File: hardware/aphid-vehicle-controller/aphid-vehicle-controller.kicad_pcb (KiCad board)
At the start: 4 copper layers, 19 parts, among them J1 ModICE ME-MX 24, J2 Conn_ST_STDC14, U1 STM32F405RGTx, U2 TJA1042T-3, U3 TJA1042T-3

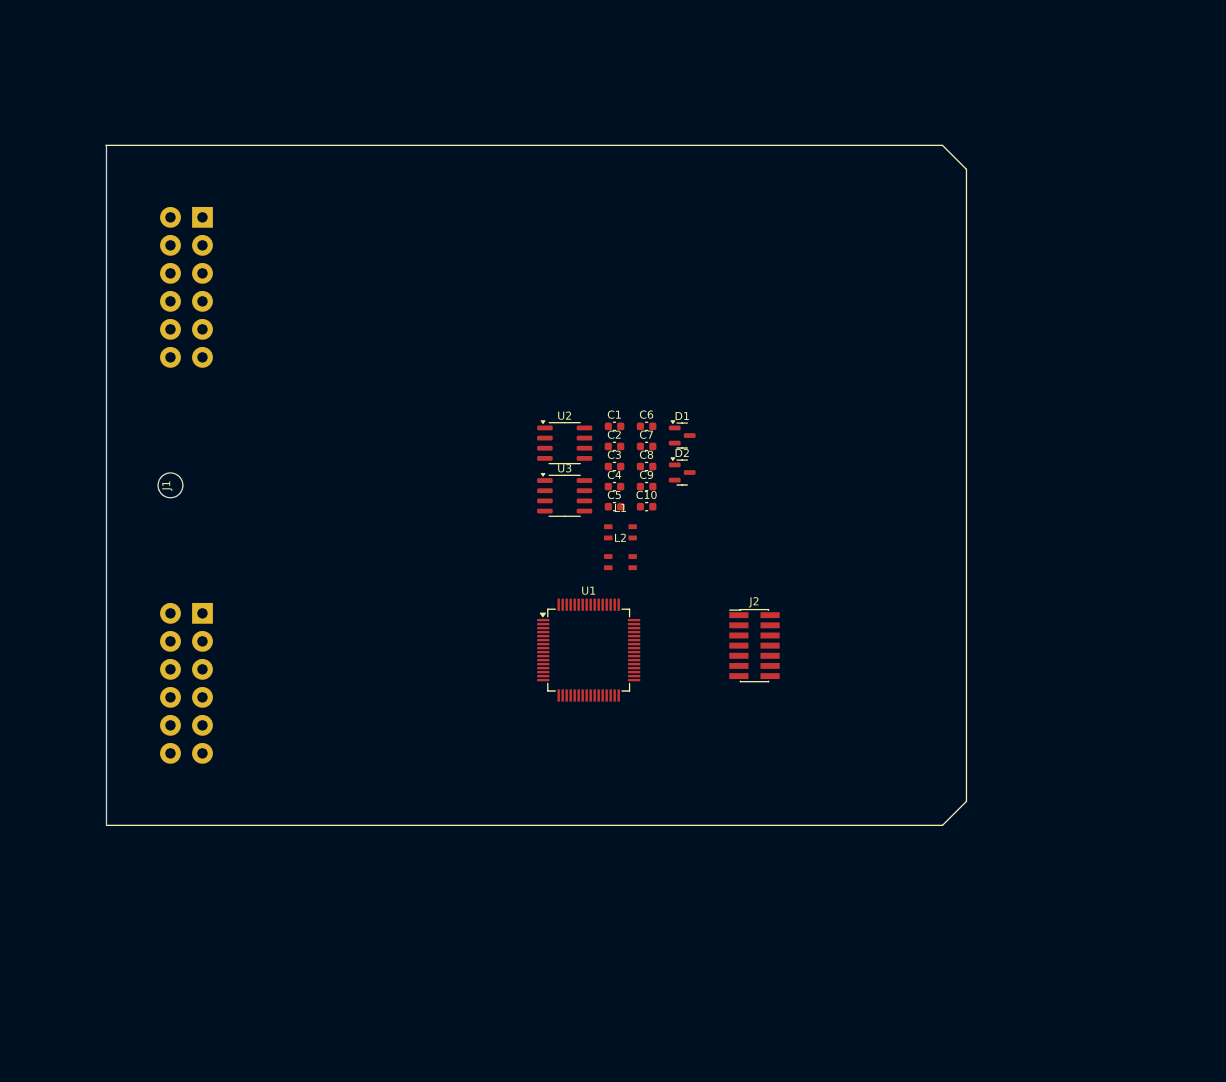
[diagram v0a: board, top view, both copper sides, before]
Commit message: feat: changed to STM32G4xx series MCU
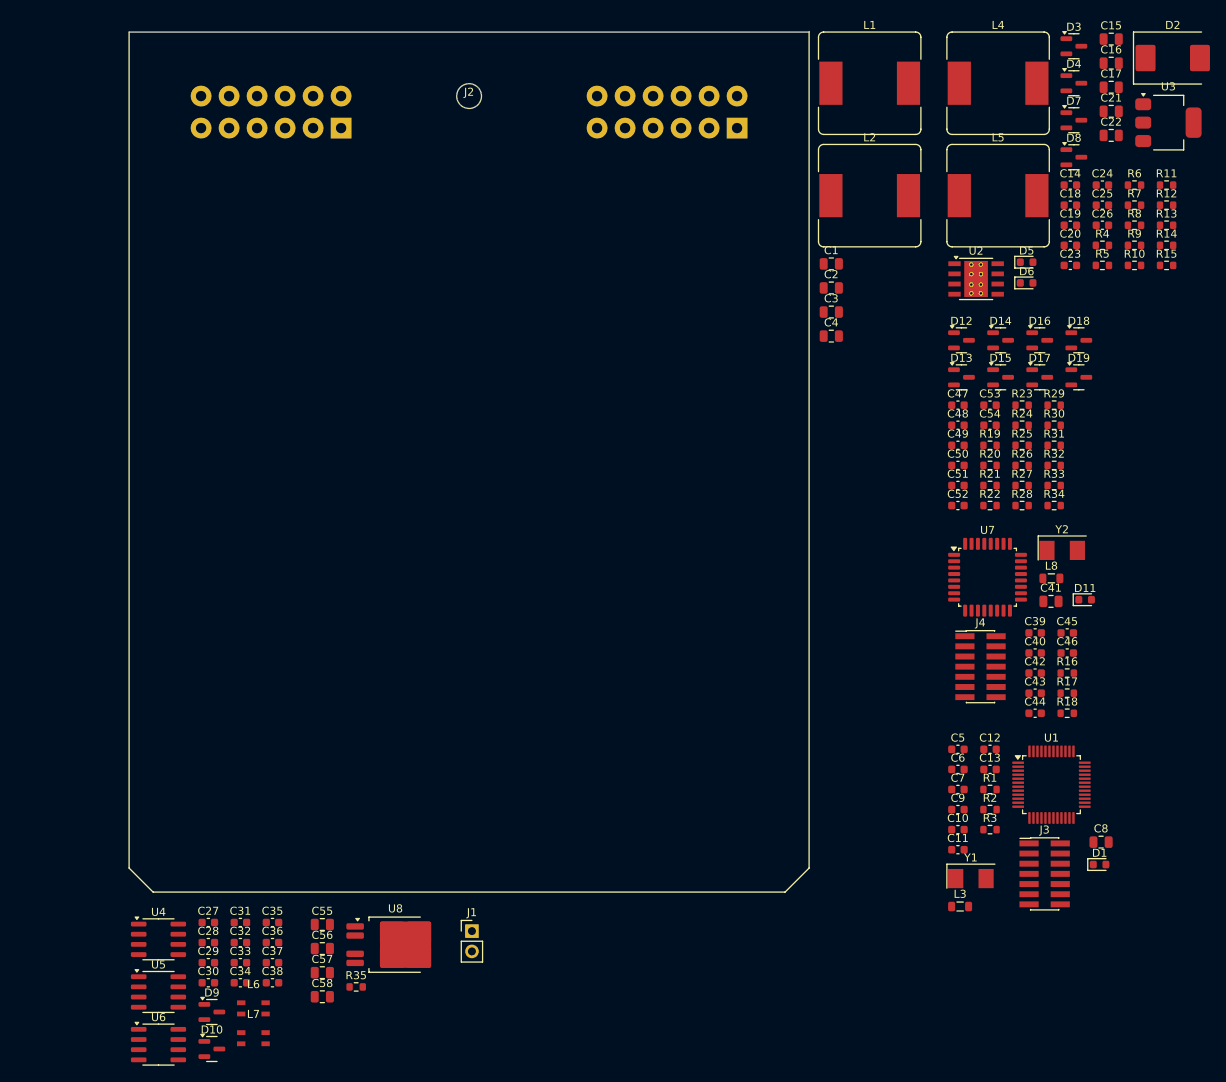
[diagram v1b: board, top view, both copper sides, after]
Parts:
- added C11: 22p, Capacitor_SMD:C_0603_1608Metric, F.Cu at (202.5, 144.2)
- added C12: 22p, Capacitor_SMD:C_0603_1608Metric, F.Cu at (206.5, 131.7)
- added C13: 100nF, Capacitor_SMD:C_0603_1608Metric, F.Cu at (206.5, 134.2)
- added C14: 10nF, Capacitor_SMD:C_0603_1608Metric, F.Cu at (216.5, 61.1)
- added C15: 10 uF, Capacitor_SMD:C_0805_2012Metric, F.Cu at (221.6, 42.9)
- added C16: 10 uF, Capacitor_SMD:C_0805_2012Metric, F.Cu at (221.6, 45.9)
- added C17: 10 uF, Capacitor_SMD:C_0805_2012Metric, F.Cu at (221.6, 48.9)
- added C18: 1 uF, Capacitor_SMD:C_0603_1608Metric, F.Cu at (216.5, 63.6)
- added C19: 100uF, Capacitor_SMD:C_0603_1608Metric, F.Cu at (216.5, 66.1)
- added C20: 1 uF, Capacitor_SMD:C_0603_1608Metric, F.Cu at (216.5, 68.7)
- added C21: 10uF, Capacitor_SMD:C_0805_2012Metric, F.Cu at (221.6, 51.9)
- added C22: 10uF, Capacitor_SMD:C_0805_2012Metric, F.Cu at (221.6, 54.9)
- added C23: 100nF, Capacitor_SMD:C_0603_1608Metric, F.Cu at (216.5, 71.2)
- added C24: 1uF, Capacitor_SMD:C_0603_1608Metric, F.Cu at (220.5, 61.1)
- added C25: 1uF, Capacitor_SMD:C_0603_1608Metric, F.Cu at (220.5, 63.6)
- added C26: 100nF, Capacitor_SMD:C_0603_1608Metric, F.Cu at (220.5, 66.1)
- added C27: 100 nF, Capacitor_SMD:C_0603_1608Metric, F.Cu at (108.8, 153.3)
- added C28: 100 nF, Capacitor_SMD:C_0603_1608Metric, F.Cu at (108.8, 155.8)
- added C29: 100 nF, Capacitor_SMD:C_0603_1608Metric, F.Cu at (108.8, 158.3)
- added C30: 33 pF, Capacitor_SMD:C_0603_1608Metric, F.Cu at (108.8, 160.8)
- added C31: 100 nF, Capacitor_SMD:C_0603_1608Metric, F.Cu at (112.8, 153.3)
- added C32: 100 nF, Capacitor_SMD:C_0603_1608Metric, F.Cu at (112.8, 155.8)
- added C33: 100 nF, Capacitor_SMD:C_0603_1608Metric, F.Cu at (112.8, 158.3)
- added C34: 33 pF, Capacitor_SMD:C_0603_1608Metric, F.Cu at (112.8, 160.8)
- added C35: 33 pF, Capacitor_SMD:C_0603_1608Metric, F.Cu at (116.8, 153.3)
- added C36: 33 pF, Capacitor_SMD:C_0603_1608Metric, F.Cu at (116.8, 155.8)
- added C37: 33 pF, Capacitor_SMD:C_0603_1608Metric, F.Cu at (116.8, 158.3)
- added C38: 33 pF, Capacitor_SMD:C_0603_1608Metric, F.Cu at (116.8, 160.8)
- added C39: 100nF, Capacitor_SMD:C_0603_1608Metric, F.Cu at (212.1, 117.1)
- added C40: 100nF, Capacitor_SMD:C_0603_1608Metric, F.Cu at (212.1, 119.6)
- added C41: 4.7uF, Capacitor_SMD:C_0805_2012Metric, F.Cu at (214.1, 113.2)
- added C42: 1uF, Capacitor_SMD:C_0603_1608Metric, F.Cu at (212.1, 122.1)
- added C43: 100nF, Capacitor_SMD:C_0603_1608Metric, F.Cu at (212.1, 124.6)
- added C44: 22p, Capacitor_SMD:C_0603_1608Metric, F.Cu at (212.1, 127.1)
- added C45: 22p, Capacitor_SMD:C_0603_1608Metric, F.Cu at (216.1, 117.1)
- added C46: 100nF, Capacitor_SMD:C_0603_1608Metric, F.Cu at (216.1, 119.6)
- added C47: 1uF, Capacitor_SMD:C_0603_1608Metric, F.Cu at (202.5, 88.6)
- added C48: 1uF, Capacitor_SMD:C_0603_1608Metric, F.Cu at (202.5, 91.1)
- added C49: 1uF, Capacitor_SMD:C_0603_1608Metric, F.Cu at (202.5, 93.7)
- added C50: 1uF, Capacitor_SMD:C_0603_1608Metric, F.Cu at (202.5, 96.2)
- added C51: 1uF, Capacitor_SMD:C_0603_1608Metric, F.Cu at (202.5, 98.7)
- added C52: 1uF, Capacitor_SMD:C_0603_1608Metric, F.Cu at (202.5, 101.2)
- added C53: 1uF, Capacitor_SMD:C_0603_1608Metric, F.Cu at (206.5, 88.6)
- added C54: 1uF, Capacitor_SMD:C_0603_1608Metric, F.Cu at (206.5, 91.1)
- added C55: 10uF, Capacitor_SMD:C_0805_2012Metric, F.Cu at (123.0, 153.6)
- added C56: 10uF, Capacitor_SMD:C_0805_2012Metric, F.Cu at (123.0, 156.6)
- added C57: 10uF, Capacitor_SMD:C_0805_2012Metric, F.Cu at (123.0, 159.6)
- added C58: 10uF, Capacitor_SMD:C_0805_2012Metric, F.Cu at (123.0, 162.6)
- added D10: NUP2105L, Package_TO_SOT_SMD:SOT-23, F.Cu at (109.2, 169.1)
- added D11: MONITOR STATUS, LED_SMD:LED_0603_1608Metric, F.Cu at (218.4, 113.0)
- added D12: BZX84C3V6, Package_TO_SOT_SMD:SOT-23, F.Cu at (202.9, 80.5)
- added D13: BZX84C3V6, Package_TO_SOT_SMD:SOT-23, F.Cu at (202.9, 85.2)
- added D14: BZX84C3V6, Package_TO_SOT_SMD:SOT-23, F.Cu at (207.8, 80.5)
- added D15: BZX84C3V6, Package_TO_SOT_SMD:SOT-23, F.Cu at (207.8, 85.2)
- added D16: BZX84C3V6, Package_TO_SOT_SMD:SOT-23, F.Cu at (212.7, 80.5)
- added D17: BZX84C3V6, Package_TO_SOT_SMD:SOT-23, F.Cu at (212.7, 85.2)
- added D18: BZX84C3V6, Package_TO_SOT_SMD:SOT-23, F.Cu at (217.6, 80.5)
- added D19: BZX84C3V6, Package_TO_SOT_SMD:SOT-23, F.Cu at (217.6, 85.2)
- added D3: BAT54C, Package_TO_SOT_SMD:SOT-23, F.Cu at (217.0, 43.8)
- added D4: BZX84C3V6, Package_TO_SOT_SMD:SOT-23, F.Cu at (217.0, 48.4)
- added D5: 5V PWR, LED_SMD:LED_0603_1608Metric, F.Cu at (211.1, 70.8)
- added D6: 3V3 PWR, LED_SMD:LED_0603_1608Metric, F.Cu at (211.1, 73.3)
- added D7: BZX84C3V6, Package_TO_SOT_SMD:SOT-23, F.Cu at (217.0, 53.0)
- added D8: BZX84C3V6, Package_TO_SOT_SMD:SOT-23, F.Cu at (217.0, 57.6)
- added D9: NUP2105L, Package_TO_SOT_SMD:SOT-23, F.Cu at (109.2, 164.5)
- added J3: MAIN_DEBUG, Connector_PinHeader_1.27mm:PinHeader_2x07_P1.27mm_Vertical_SMD, F.Cu at (213.3, 147.2)
- added J4: MONITOR_DEBUG, Connector_PinHeader_1.27mm:PinHeader_2x07_P1.27mm_Vertical_SMD, F.Cu at (205.3, 121.3)
- added L3: L, Inductor_SMD:L_0805_2012Metric, F.Cu at (202.8, 151.3)
- added L4: L, Inductor_SMD:L_Bourns_SRR1260, F.Cu at (207.5, 48.4)
- added L5: 22 uH, Inductor_SMD:L_Bourns_SRR1260, F.Cu at (207.5, 62.4)
- added L6: ACT1210D, aphid:ACT1210D, F.Cu at (114.4, 164.0)
- added L7: ACT1210D, aphid:ACT1210D, F.Cu at (114.4, 167.8)
- added L8: L, Inductor_SMD:L_0805_2012Metric, F.Cu at (214.2, 110.3)
- added R1: 22, Resistor_SMD:R_0603_1608Metric, F.Cu at (206.5, 136.7)
- added R10: 10k, Resistor_SMD:R_0603_1608Metric, F.Cu at (224.6, 71.2)
- added R11: 220, Resistor_SMD:R_0603_1608Metric, F.Cu at (228.6, 61.1)
- added R12: 38k, Resistor_SMD:R_0603_1608Metric, F.Cu at (228.6, 63.6)
- added R13: 10k, Resistor_SMD:R_0603_1608Metric, F.Cu at (228.6, 66.1)
- added R14: 38k, Resistor_SMD:R_0603_1608Metric, F.Cu at (228.6, 68.7)
- added R15: 10k, Resistor_SMD:R_0603_1608Metric, F.Cu at (228.6, 71.2)
- added R16: 22, Resistor_SMD:R_0603_1608Metric, F.Cu at (216.1, 122.1)
- added R17: 10k, Resistor_SMD:R_0603_1608Metric, F.Cu at (216.1, 124.6)
- added R18: 10k, Resistor_SMD:R_0603_1608Metric, F.Cu at (216.1, 127.1)
- added R19: 5.1k, Resistor_SMD:R_0603_1608Metric, F.Cu at (206.5, 93.7)
- added R2: 10k, Resistor_SMD:R_0603_1608Metric, F.Cu at (206.5, 139.2)
- added R20: 5.1k, Resistor_SMD:R_0603_1608Metric, F.Cu at (206.5, 96.2)
- added R21: 10k, Resistor_SMD:R_0603_1608Metric, F.Cu at (206.5, 98.7)
- added R22: 10k, Resistor_SMD:R_0603_1608Metric, F.Cu at (206.5, 101.2)
- added R23: 5.1k, Resistor_SMD:R_0603_1608Metric, F.Cu at (210.5, 88.6)
- added R24: 5.1k, Resistor_SMD:R_0603_1608Metric, F.Cu at (210.5, 91.1)
- added R25: 10k, Resistor_SMD:R_0603_1608Metric, F.Cu at (210.5, 93.7)
- added R26: 10k, Resistor_SMD:R_0603_1608Metric, F.Cu at (210.5, 96.2)
- added R27: 5.1k, Resistor_SMD:R_0603_1608Metric, F.Cu at (210.5, 98.7)
- added R28: 5.1k, Resistor_SMD:R_0603_1608Metric, F.Cu at (210.5, 101.2)
- added R29: 10k, Resistor_SMD:R_0603_1608Metric, F.Cu at (214.5, 88.6)
- added R3: 10k, Resistor_SMD:R_0603_1608Metric, F.Cu at (206.5, 141.7)
- added R30: 10k, Resistor_SMD:R_0603_1608Metric, F.Cu at (214.5, 91.1)
- added R31: 5.1k, Resistor_SMD:R_0603_1608Metric, F.Cu at (214.5, 93.7)
- added R32: 5.1k, Resistor_SMD:R_0603_1608Metric, F.Cu at (214.5, 96.2)
- added R33: 10k, Resistor_SMD:R_0603_1608Metric, F.Cu at (214.5, 98.7)
- added R34: 10k, Resistor_SMD:R_0603_1608Metric, F.Cu at (214.5, 101.2)
- added R35: R, Resistor_SMD:R_0603_1608Metric, F.Cu at (127.3, 161.3)
- added R4: R, Resistor_SMD:R_0603_1608Metric, F.Cu at (220.5, 68.7)
- added R5: 38k, Resistor_SMD:R_0603_1608Metric, F.Cu at (220.5, 71.2)
- added R6: R, Resistor_SMD:R_0603_1608Metric, F.Cu at (224.6, 61.1)
- added R7: 10k, Resistor_SMD:R_0603_1608Metric, F.Cu at (224.6, 63.6)
- added R8: 38k, Resistor_SMD:R_0603_1608Metric, F.Cu at (224.6, 66.1)
- added R9: 10k, Resistor_SMD:R_0603_1608Metric, F.Cu at (224.6, 68.7)
- added U4: TJA1042T-3, Package_SO:SOIC-8_3.9x4.9mm_P1.27mm, F.Cu at (102.6, 155.4)
- added U5: TJA1042T-3, Package_SO:SOIC-8_3.9x4.9mm_P1.27mm, F.Cu at (102.6, 162.0)
- added U6: TJA1042T-3, Package_SO:SOIC-8_3.9x4.9mm_P1.27mm, F.Cu at (102.6, 168.6)
- added U7: STM32G431KBTx, Package_QFP:LQFP-32_7x7mm_P0.8mm, F.Cu at (206.2, 110.1)
- added U8: BTS6143D, Package_TO_SOT_SMD:TO-252-4, F.Cu at (132.2, 156.1)
- added Y1: 8 MHz, aphid:ABM3-x.xxxMHZ-D2Y-T, F.Cu at (204.1, 147.8)
- added Y2: 8 MHz, aphid:ABM3-x.xxxMHZ-D2Y-T, F.Cu at (215.5, 106.8)
- C1, C2, C3, C4: value 33 pF -> 10uF; footprint Capacitor_SMD:C_0603_1608Metric -> Capacitor_SMD:C_0805_2012Metric
- C10, C7: value 100 nF -> 100nF
- C5, C6: value 33 pF -> 100nF
- C8: value 100 nF -> 4.7uF; footprint Capacitor_SMD:C_0603_1608Metric -> Capacitor_SMD:C_0805_2012Metric
- C9: value 100 nF -> 1uF
- D1: value NUP2105L -> STATUS; footprint Package_TO_SOT_SMD:SOT-23 -> LED_SMD:LED_0603_1608Metric
- D2: value NUP2105L -> B340; footprint Package_TO_SOT_SMD:SOT-23 -> Diode_SMD:D_SMC
- J1: value ModICE ME-MX 24 -> MONITOR UART; footprint aphid-vehicle-controller:ModICE_ME-MX_24 -> Connector_PinHeader_2.54mm:PinHeader_1x02_P2.54mm_Vertical
- J2: value Conn_ST_STDC14 -> ModICE ME-MX 24; footprint Connector_PinHeader_1.27mm:PinHeader_2x07_P1.27mm_Vertical_SMD -> aphid:ModICE_ME-MX_24
- L1, L2: value ACT1210D -> L; footprint aphid-vehicle-controller:ACT1210D -> Inductor_SMD:L_Bourns_SRR1260
- U1: value STM32F405RGTx -> STM32G491CETx; footprint Package_QFP:LQFP-64_10x10mm_P0.5mm -> Package_QFP:LQFP-48_7x7mm_P0.5mm
- U2: value TJA1042T-3 -> TPS5430DDA; footprint Package_SO:SOIC-8_3.9x4.9mm_P1.27mm -> Package_SO:TI_SO-PowerPAD-8_ThermalVias
- U3: value TJA1042T-3 -> AMS1117-3.3; footprint Package_SO:SOIC-8_3.9x4.9mm_P1.27mm -> Package_TO_SOT_SMD:SOT-223-3_TabPin2
- moved U3 88.7 mm to (228.8, 53.3)
- moved D2 80.3 mm to (229.3, 45.2)
- moved J2 77.4 mm to (141.4, 50.0)
- moved D1 74.8 mm to (220.2, 146.1)
- moved C8 73.7 mm to (220.4, 143.2)
- moved J1 67.3 mm to (141.7, 154.4), turned to 0 degrees
- moved L1 64.2 mm to (191.5, 48.4)
- moved U1 60.2 mm to (214.2, 136.1)
- moved C6 57.9 mm to (202.5, 134.2)
- moved C7 57.9 mm to (202.5, 136.7)
- moved C10 56.1 mm to (202.5, 141.7)
- moved C9 56.1 mm to (202.5, 139.2)
- moved L2 55.4 mm to (191.5, 62.4)
- moved U2 55.4 mm to (204.8, 72.9)
- moved C5 52.6 mm to (202.5, 131.7)
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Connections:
- C1 pad 1: Net-(U2-CANH) -> Net-(J2A-L9)
- C10 pad 1: +3.3V -> /MCU/MAIN_VDDA
- C2 pad 1: Net-(U2-CANH) -> +5V
- C2 pad 2: Net-(U2-CANL) -> GND
- C3 pad 1: Net-(U2-CANL) -> Net-(J2B-R9)
- C4 pad 1: Net-(U3-CANH) -> +5V
- C5 pad 1: Net-(U3-CANL) -> +3.3V
- C6 pad 1: Net-(U3-CANH) -> +3.3V
- C6 pad 2: Net-(U3-CANL) -> GND
- C7 pad 1: +5V -> +3.3V
- C8 pad 1: +5V -> +3.3V
- C9 pad 1: +3.3V -> /MCU/MAIN_VDDA
- D1 pad 1: Net-(U2-CANH) -> GND
- D1 pad 2: Net-(U2-CANL) -> Net-(D1-A)
- D2 pad 1: Net-(U3-CANH) -> Net-(D2-K)
- D2 pad 2: Net-(U3-CANL) -> GND
- J1 pad 1: GND -> /MCU/MONITOR_UART_TX
- J1 pad 2: /CAN/CAN1_LOW -> /MCU/MONITOR_UART_RX
- J2 pad 1: unconnected-(J2-NC-Pad1) -> GND
- J2 pad 10: unconnected-(J2-JTDI/NC-Pad10) -> /Connectors/ACC2
- J2 pad 11: unconnected-(J2-GNDDetect-Pad11) -> /Connectors/ACC1
- J2 pad 12: unconnected-(J2-~{RST}-Pad12) -> /Connectors/VIN
- J2 pad 13: unconnected-(J2-VCP_RX-Pad13) -> GND
- J2 pad 14: unconnected-(J2-VCP_TX-Pad14) -> /CAN/CAN2_LOW
- J2 pad 2: unconnected-(J2-NC-Pad2) -> /CAN/CAN1_LOW
- J2 pad 3: unconnected-(J2-VCC-Pad3) -> /CAN/CAN1_HIGH
- J2 pad 4: unconnected-(J2-JTMS/SWDIO-Pad4) -> /Connectors/BRAKE2
- J2 pad 5: Net-(J2-GND-Pad5) -> /Connectors/BRAKE1
- J2 pad 6: unconnected-(J2-JCLK/SWCLK-Pad6) -> /Connectors/VIN
- J2 pad 7: Net-(J2-GND-Pad5) -> GND
- J2 pad 9: unconnected-(J2-JRCLK/NC-Pad9) -> Net-(J2A-L9)
- L1 pad 1: Net-(U2-CANH) -> +5V
- L1 pad 2: Net-(U2-CANL) -> Net-(J2A-L9)
- L2 pad 1: Net-(U3-CANH) -> +5V
- L2 pad 2: Net-(U3-CANL) -> Net-(J2B-R9)
- U1 pad 1: unconnected-(U1-VBAT-Pad1) -> +3.3V
- U1 pad 16: unconnected-(U1-PA2-Pad16) -> /MCU/POWER_KEEPALIVE
- U1 pad 18: Net-(U1-VSS-Pad18) -> unconnected-(U1-PB2-Pad18)
- U1 pad 19: unconnected-(U1-VDD-Pad19) -> GND
- U1 pad 20: unconnected-(U1-PA4-Pad20) -> /MCU/MAIN_VDDA
- U1 pad 21: unconnected-(U1-PA5-Pad21) -> /MCU/MAIN_VDDA
- U1 pad 22: unconnected-(U1-PA6-Pad22) -> /MCU/MAIN_DBG_TX
- U1 pad 23: unconnected-(U1-PA7-Pad23) -> GND
- U1 pad 24: unconnected-(U1-PC4-Pad24) -> +3.3V
- U1 pad 25: unconnected-(U1-PC5-Pad25) -> /MCU/MAIN_DBG_RX
- U1 pad 26: unconnected-(U1-PB0-Pad26) -> /CAN/CAN2_RX
- U1 pad 27: unconnected-(U1-PB1-Pad27) -> /CAN/CAN2_TX
- U1 pad 31: unconnected-(U1-VCAP_1-Pad31) -> /MCU/MONITOR_UART_TX
- U1 pad 32: unconnected-(U1-VDD-Pad32) -> /MCU/MONITOR_UART_RX
- U1 pad 33: unconnected-(U1-PB12-Pad33) -> /CAN/CAN1_RX
- U1 pad 34: unconnected-(U1-PB13-Pad34) -> /CAN/CAN1_TX
- U1 pad 35: unconnected-(U1-PB14-Pad35) -> GND
- U1 pad 36: unconnected-(U1-PB15-Pad36) -> +3.3V
- U1 pad 37: unconnected-(U1-PC6-Pad37) -> /MCU/MAIN_SWDIO
- U1 pad 38: unconnected-(U1-PC7-Pad38) -> /MCU/MAIN_SWCLK
- U1 pad 40: unconnected-(U1-PC9-Pad40) -> /MCU/MAIN_SWO
- U1 pad 47: unconnected-(U1-VCAP_2-Pad47) -> GND
- U1 pad 48: unconnected-(U1-VDD-Pad48) -> +3.3V
- U1 pad 5: unconnected-(U1-PH0-Pad5) -> /MCU/MAIN_OSC_IN
- U1 pad 6: unconnected-(U1-PH1-Pad6) -> /MCU/MAIN_OSC_OUT
- U1 pad 7: unconnected-(U1-NRST-Pad7) -> /MCU/MAIN_NRST
- U2 pad 1: /CAN/CAN1_TX -> Net-(U2-BOOT)
- U2 pad 2: GND -> unconnected-(U2-NC-Pad2)
- U2 pad 3: +5V -> unconnected-(U2-NC-Pad3)
- U2 pad 4: /CAN/CAN1_RX -> Net-(U2-VSENSE)
- U2 pad 5: +3.3V -> Net-(U2-EN)
- U2 pad 6: Net-(U2-CANL) -> GND
- U2 pad 7: Net-(U2-CANH) -> +12V
- U2 pad 8: GND -> Net-(D2-K)
- U3 pad 1: /CAN/CAN2_TX -> GND
- U3 pad 2: GND -> +3.3V

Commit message: feat: changed to a more modern DCDC
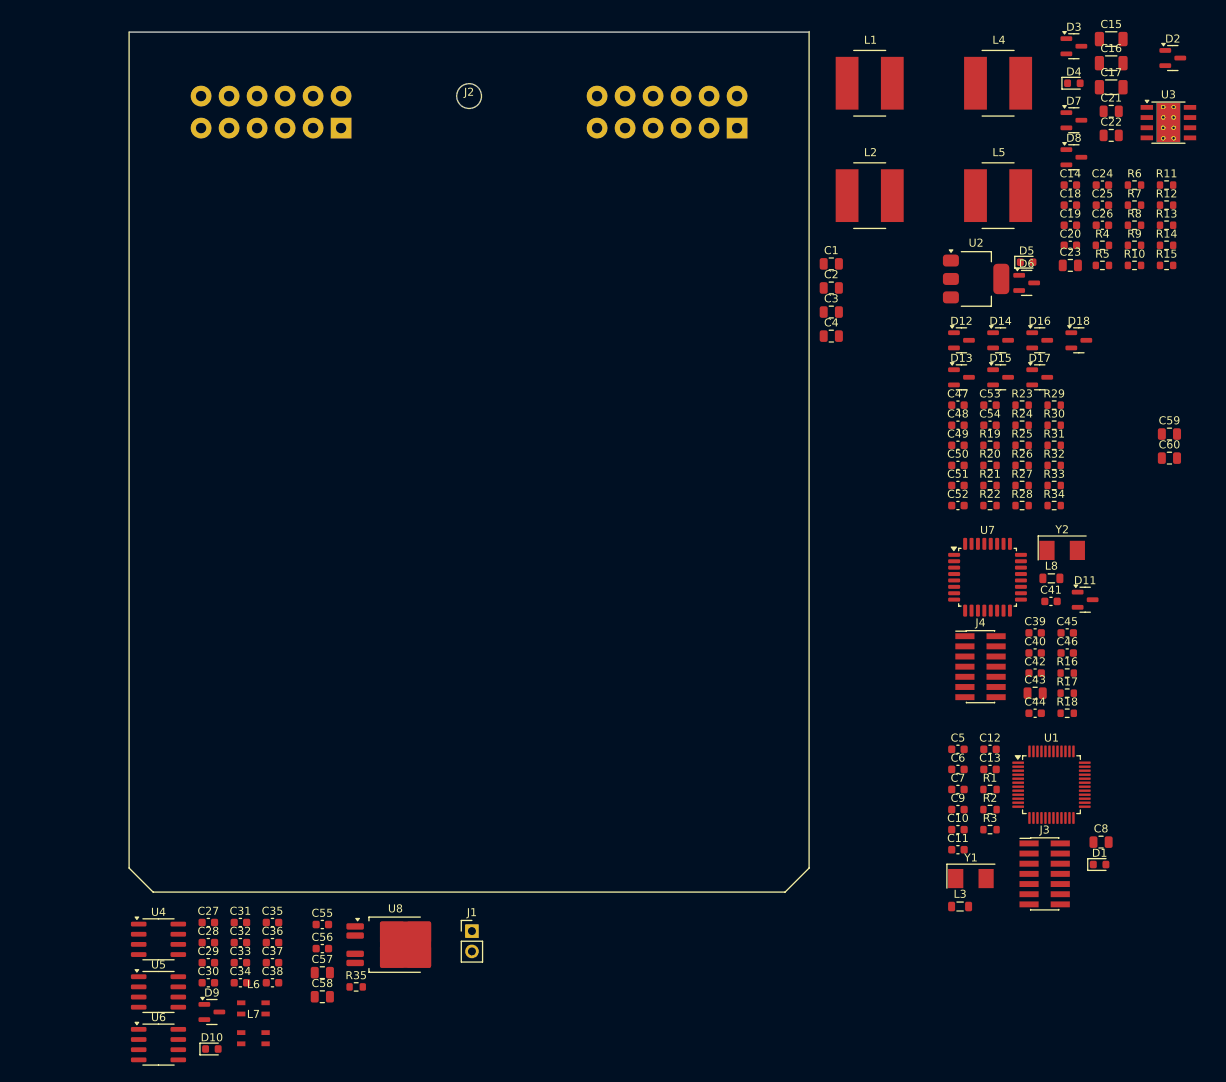
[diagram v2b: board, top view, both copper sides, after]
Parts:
- removed D19: BZX84C3V6, Package_TO_SOT_SMD:SOT-23
- added C59: 10uF, Capacitor_SMD:C_0805_2012Metric, F.Cu at (228.9, 92.2)
- added C60: 10uF, Capacitor_SMD:C_0805_2012Metric, F.Cu at (228.9, 95.2)
- C14: value 10nF -> 100nF
- C15, C16, C17: value 10 uF -> 10 uF 50V; footprint Capacitor_SMD:C_0805_2012Metric -> Capacitor_SMD:C_1206_3216Metric
- C18, C20: value 1 uF -> 100nF
- C19: value 100uF -> 6.8pF
- C21, C22: value 10uF -> 22uF
- C23: value 100nF -> 22uF; footprint Capacitor_SMD:C_0603_1608Metric -> Capacitor_SMD:C_0805_2012Metric
- C25, C42, C48: value 1uF -> 100nF
- C26: value 100nF -> 1uF
- C27: value 100 nF -> 1uF
- C28: value 100 nF -> 100nF
- C30, C34, C35: value 33 pF -> 100 nF
- C32: value 100 nF -> 33 pF
- C39, C40: value 100nF -> 33 pF
- C41: value 4.7uF -> 100nF; footprint Capacitor_SMD:C_0805_2012Metric -> Capacitor_SMD:C_0603_1608Metric
- C43: value 100nF -> 4.7uF; footprint Capacitor_SMD:C_0603_1608Metric -> Capacitor_SMD:C_0805_2012Metric
- C44: value 22p -> 1uF
- C45: value 22p -> 100nF
- C46: value 100nF -> 22p
- C47: value 1uF -> 22p
- C55, C56: value 10uF -> 1uF; footprint Capacitor_SMD:C_0805_2012Metric -> Capacitor_SMD:C_0603_1608Metric
- D10: value NUP2105L -> MONITOR STATUS; footprint Package_TO_SOT_SMD:SOT-23 -> LED_SMD:LED_0603_1608Metric
- D11: value MONITOR STATUS -> BZX84C3V6; footprint LED_SMD:LED_0603_1608Metric -> Package_TO_SOT_SMD:SOT-23
- D2: value B340 -> BAT54C; footprint Diode_SMD:D_SMC -> Package_TO_SOT_SMD:SOT-23
- D3: value BAT54C -> BZX84C3V6
- D4: value BZX84C3V6 -> 5V PWR; footprint Package_TO_SOT_SMD:SOT-23 -> LED_SMD:LED_0603_1608Metric
- D5: value 5V PWR -> 3V3 PWR
- D6: value 3V3 PWR -> BZX84C3V6; footprint LED_SMD:LED_0603_1608Metric -> Package_TO_SOT_SMD:SOT-23
- D8: value BZX84C3V6 -> NUP2105L
- L1, L2, L4: value L -> 2.2uH; footprint Inductor_SMD:L_Bourns_SRR1260 -> Inductor_SMD:L_Bourns_SRN8040TA
- L5: value 22 uH -> 2.2uH; footprint Inductor_SMD:L_Bourns_SRR1260 -> Inductor_SMD:L_Bourns_SRN8040TA
- R4: value R -> 100k
- R5: value 38k -> 24.9k
- R6: value R -> 38k
- U2: value TPS5430DDA -> AMS1117-3.3; footprint Package_SO:TI_SO-PowerPAD-8_ThermalVias -> Package_TO_SOT_SMD:SOT-223-3_TabPin2
- U3: value AMS1117-3.3 -> LMR33630BDDA; footprint Package_TO_SOT_SMD:SOT-223-3_TabPin2 -> Package_SO:Texas_HSOP-8-1EP_3.9x4.9mm_P1.27mm_ThermalVias
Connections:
- C14 pad 1: Net-(U2-BOOT) -> Net-(U3-BOOT)
- C14 pad 2: Net-(D2-K) -> Net-(U3-SW)
- C19 pad 2: GND -> Net-(U3-FB)
- C22 pad 1: +3.3V -> +5V
- C23 pad 1: Net-(U2-EN) -> +3.3V
- C24 pad 1: /MCU/VIN_SENSE -> Net-(U3-VCC)
- C25 pad 1: /MCU/IGNITION_SENSE -> Net-(U3-EN)
- C26 pad 1: /MCU/CRANK_SENSE -> /MCU/VIN_SENSE
- C27 pad 1: +5V -> /MCU/IGNITION_SENSE
- C28 pad 1: +5V -> /MCU/CRANK_SENSE
- C30 pad 1: Net-(U4-CANH) -> +5V
- C30 pad 2: Net-(U4-CANL) -> GND
- C31 pad 1: +3.3V -> +5V
- C32 pad 1: +3.3V -> Net-(U4-CANH)
- C32 pad 2: GND -> Net-(U4-CANL)
- C34 pad 1: Net-(U4-CANH) -> +3.3V
- C35 pad 1: Net-(U4-CANL) -> +3.3V
- C36 pad 1: Net-(U6-CANH) -> Net-(U4-CANH)
- C36 pad 2: Net-(U6-CANL) -> GND
- C37 pad 1: Net-(U6-CANH) -> Net-(U4-CANL)
- C38 pad 1: Net-(U6-CANL) -> Net-(U6-CANH)
- C38 pad 2: GND -> Net-(U6-CANL)
- C39 pad 1: +3.3V -> Net-(U6-CANH)
- C40 pad 1: +3.3V -> Net-(U6-CANL)
- C42 pad 1: /Monitor/MONITOR_VDDA -> +3.3V
- C43 pad 1: /Monitor/MONITOR_VDDA -> +3.3V
- C44 pad 1: /Monitor/MONITOR_OSC_IN -> /Monitor/MONITOR_VDDA
- C45 pad 1: Net-(C45-Pad1) -> /Monitor/MONITOR_VDDA
- C46 pad 1: /Monitor/MONITOR_NRST -> /Monitor/MONITOR_OSC_IN
- C47 pad 1: /Inputs/BRAKE1_FILTERED -> Net-(C47-Pad1)
- C48 pad 1: /Inputs/ACC1_FILTERED -> /Monitor/MONITOR_NRST
- C49 pad 1: /Inputs/BRAKE2_FILTERED -> /Inputs/BRAKE1_FILTERED
- C50 pad 1: /Inputs/ACC2_FILTERED -> /Inputs/ACC1_FILTERED
- C51 pad 1: /Inputs/DIR_F1_FILTERED -> /Inputs/BRAKE2_FILTERED
- C52 pad 1: /Inputs/DIR_R1_FILTERED -> /Inputs/ACC2_FILTERED
- C53 pad 1: /Inputs/DIR_F2_FILTERED -> /Inputs/DIR_F1_FILTERED
- C54 pad 1: /Inputs/DIR_R2_FILTERED -> /Inputs/DIR_R1_FILTERED
- C55 pad 1: +12V -> /Inputs/DIR_F2_FILTERED
- C56 pad 1: +12V -> /Inputs/DIR_R2_FILTERED
- D10 pad 1: Net-(U6-CANH) -> GND
- D10 pad 2: Net-(U6-CANL) -> Net-(D10-A)
- D11 pad 2: Net-(D11-A) -> unconnected-(D11-NC-Pad2)
- D12 pad 3: /Inputs/BRAKE1_FILTERED -> /Inputs/ACC1_FILTERED
- D13 pad 3: /Inputs/ACC1_FILTERED -> /Inputs/BRAKE2_FILTERED
- D14 pad 3: /Inputs/BRAKE2_FILTERED -> /Inputs/ACC2_FILTERED
- D15 pad 3: /Inputs/ACC2_FILTERED -> /Inputs/DIR_F1_FILTERED
- D16 pad 3: /Inputs/DIR_F1_FILTERED -> /Inputs/DIR_R1_FILTERED
- D17 pad 3: /Inputs/DIR_R1_FILTERED -> /Inputs/DIR_F2_FILTERED
- D18 pad 3: /Inputs/DIR_F2_FILTERED -> /Inputs/DIR_R2_FILTERED
- D2 pad 1: Net-(D2-K) -> /MCU/POWER_KEEPALIVE
- D2 pad 2: GND -> Net-(D2-Pad2)
- D3 pad 1: /MCU/POWER_KEEPALIVE -> GND
- D3 pad 2: Net-(D3-Pad2) -> unconnected-(D3-NC-Pad2)
- D3 pad 3: Net-(U2-EN) -> /MCU/VIN_SENSE
- D4 pad 2: unconnected-(D4-NC-Pad2) -> Net-(D4-A)
- D6 pad 2: Net-(D6-A) -> unconnected-(D6-NC-Pad2)
- D7 pad 3: /MCU/IGNITION_SENSE -> /MCU/CRANK_SENSE
- D8 pad 1: GND -> Net-(U4-CANH)
- D8 pad 2: unconnected-(D8-NC-Pad2) -> Net-(U4-CANL)
- D8 pad 3: /MCU/CRANK_SENSE -> GND
- D9 pad 1: Net-(U4-CANH) -> Net-(U6-CANH)
- D9 pad 2: Net-(U4-CANL) -> Net-(U6-CANL)
- L1 pad 1: +5V -> Net-(J2A-L9)
- L1 pad 2: Net-(J2A-L9) -> +5V
- L2 pad 1: +5V -> Net-(J2B-R9)
- L2 pad 2: Net-(J2B-R9) -> +5V
- L5 pad 1: Net-(D2-K) -> Net-(U3-SW)
- R10 pad 1: Net-(D5-A) -> Net-(D4-A)
- R11 pad 1: Net-(D6-A) -> Net-(D5-A)
- R16 pad 1: Net-(C45-Pad1) -> Net-(C47-Pad1)
- R18 pad 1: Net-(D11-A) -> Net-(D10-A)
- R4 pad 2: Net-(U2-VSENSE) -> Net-(U3-FB)
- R5 pad 1: Net-(D3-Pad2) -> Net-(U3-FB)
- R5 pad 2: /Connectors/IGNITION -> GND
- R6 pad 1: Net-(U2-VSENSE) -> Net-(D2-Pad2)
- R6 pad 2: GND -> /Connectors/IGNITION
- R7 pad 2: Net-(U2-EN) -> Net-(U3-EN)
- U2 pad 1: Net-(U2-BOOT) -> GND
- U2 pad 2: unconnected-(U2-NC-Pad2) -> +3.3V
- U2 pad 3: unconnected-(U2-NC-Pad3) -> +5V
- U3 pad 2: +3.3V -> +12V
- U3 pad 3: +5V -> Net-(U3-EN)
- Y2 pad 2: Net-(C45-Pad1) -> Net-(C47-Pad1)

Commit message: worked on routing
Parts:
- C31, C34, C35: value 100 nF -> 33 pF
- C32, C36, C37: value 33 pF -> 100 nF
- J3, J4: moved to B.Cu
- moved R13 127.2 mm to (107.1, 104.1)
- moved R12 126.0 mm to (106.7, 95.7), turned to 90 degrees
- moved R15 122.6 mm to (110.5, 104.1)
- moved R14 121.1 mm to (110.5, 95.7), turned to 90 degrees
- moved L6 117.2 mm to (170.2, 61.0), turned to 90 degrees
- moved D7 116.5 mm to (110.5, 100.3), turned to 90 degrees
- moved C34 108.5 mm to (165.6, 66.0)
- moved D6 107.8 mm to (106.7, 100.3), turned to 90 degrees
- moved C39 107.4 mm to (115.1, 71.1)
- moved L7 106.7 mm to (120.1, 61.2), turned to 90 degrees
- moved C3 105.0 mm to (87.6, 42.2), turned to -90 degrees
- moved C4 104.3 mm to (87.6, 47.3), turned to 90 degrees
- moved C40 103.5 mm to (119.4, 73.7)
- moved C35 103.3 mm to (174.0, 67.3)
- moved R35 103.1 mm to (132.5, 58.4)
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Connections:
- C30 pad 1: +5V -> +3.3V
- C31 pad 1: +5V -> Net-(U4-CANH)
- C31 pad 2: GND -> Net-(U4-CANL)
- C32 pad 1: Net-(U4-CANH) -> +5V
- C32 pad 2: Net-(U4-CANL) -> GND
- C34 pad 1: +3.3V -> Net-(U4-CANH)
- C35 pad 1: +3.3V -> Net-(U4-CANL)
- C36 pad 1: Net-(U4-CANH) -> +5V
- C37 pad 1: Net-(U4-CANL) -> +3.3V
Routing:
- added copper zone on In1.Cu, net GND
